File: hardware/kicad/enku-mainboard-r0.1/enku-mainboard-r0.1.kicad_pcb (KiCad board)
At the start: 4 copper layers, 54 x 94 mm, 156 parts, among them J1 1S LiPo + NTC, J2 Hirose DM3AT-SF-PEJM5, J3 FH34SRJ-24S-0.5SH(50), J4 FH34SRJ-6S-0.5SH(50), J5 GCT USB4105-GF-A-120, J6 4-pin pogo dock, J7 Tag-Connect TC2030-IDC-NL, J8 Pro Wireless Qi raw interface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, Q1 IRLML6346TRPBF, Q2 BSS138LT1G, Q3 BSS138LT1G, SW1 HARD POWER, SW2 BOOT / RECOVERY, SW3 BTN_PREV, SW4 BTN_NEXT, SW5 BTN_SELECT, SW6 BTN_BACK, U1 ESP32-S3-WROOM-1-N16R8, U2 TPS2121, U3 BQ25185DLHR, U4 TPS63802DLAR, U5 BMI270, U6 DRV5032FBDBZR, U7 TPS923610DRLR, U8 USBLC6-2SC6

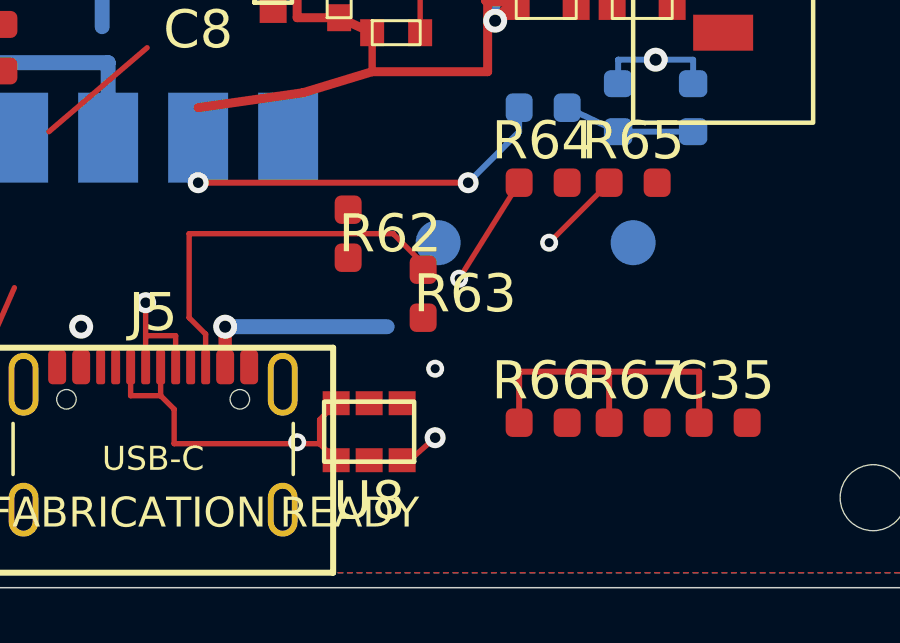
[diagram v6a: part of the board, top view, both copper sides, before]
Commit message: pcb: purge orphaned USB differential stubs
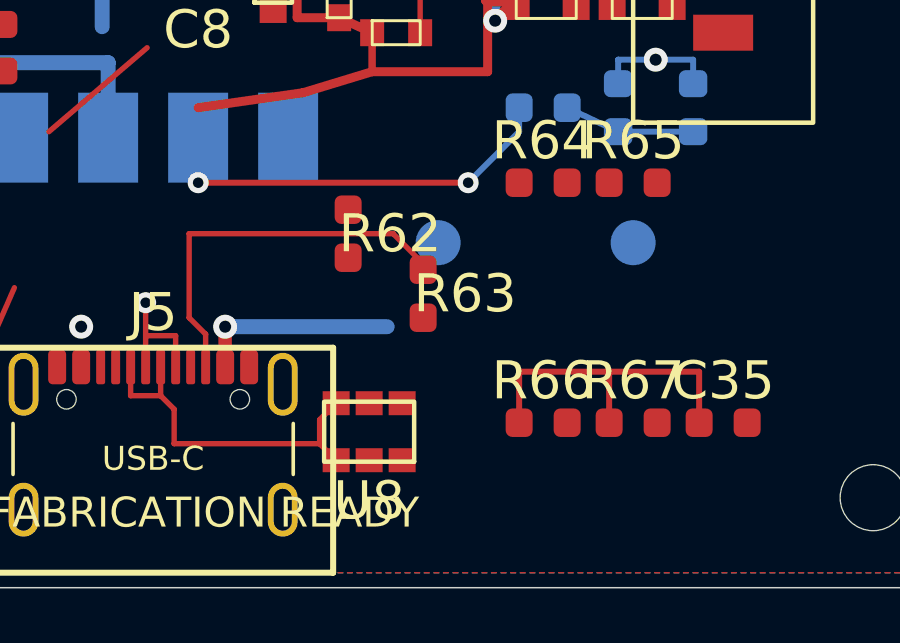
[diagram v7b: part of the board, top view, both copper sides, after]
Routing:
- net USB_DP_CONN: track 9.35 -> 4.19 mm, vias 4 -> 1
- net USB_DM_CONN: track 14.7 -> 11.9 mm, vias 2 -> 0
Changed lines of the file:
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@@
   (segment (start 46.75 105.60) (end 46.75 104.50) (width 0.18) (layer "F.Cu") (net 6))
   (via (at 46.75 104.50) (size 0.70) (drill 0.35) (layers "F.Cu" "B.Cu") (net 6))
-  (via (at 56.40 109.00) (size 0.70) (drill 0.35) (layers "F.Cu" "B.Cu") (net 6))
-  (segment (start 56.40 109.00) (end 55.55 109.75) (width 0.18) (layer "F.Cu") (net 6))
-  (segment (start 55.55 109.75) (end 55.30 109.75) (width 0.18) (layer "F.Cu") (net 6))
   (segment (start 46.25 106.645) (end 46.25 107.60) (width 0.18) (layer "F.Cu") (net 7))
   (segment (start 47.25 106.645) (end 47.25 107.60) (width 0.18) (layer "F.Cu") (net 7))
@@
   (segment (start 62.2 106.8) (end 65.2 106.8) (width 0.20) (layer "F.Cu") (net 8))
   (segment (start 65.2 106.8) (end 65.2 108.5) (width 0.20) (layer "F.Cu") (net 8))
-  (via (at 56.4 106.7) (size 0.60) (drill 0.30) (layers "F.Cu" "In1.Cu") (net 6))
   (segment (start 53.1 107.85) (end 52.55 108.4) (width 0.18) (layer "F.Cu") (net 7))
   (segment (start 52.55 108.4) (end 52.55 109.2) (width 0.18) (layer "F.Cu") (net 7))
-  (via (at 57.2 103.7) (size 0.60) (drill 0.30) (layers "F.Cu" "In1.Cu") (net 6))
-  (segment (start 57.2 103.7) (end 59.2 100.5) (width 0.18) (layer "F.Cu") (net 6))
-  (via (at 51.8 109.15) (size 0.60) (drill 0.30) (layers "F.Cu" "In1.Cu") (net 7))
-  (via (at 60.2 102.5) (size 0.60) (drill 0.30) (layers "F.Cu" "In1.Cu") (net 7))
-  (segment (start 60.2 102.5) (end 62.2 100.5) (width 0.18) (layer "F.Cu") (net 7))
   (segment (start 30.825 104) (end 25 100.6) (width 0.18) (layer "F.Cu") (net 10))
   (via (at 70.5 33.5) (size 0.60) (drill 0.30) (layers "F.Cu" "B.Cu") (net 13))

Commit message: pcb: purge isolated EPD service vias
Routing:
- net EPD_VSL: track 1.55 -> 0.00 mm, vias 2 -> 0
- net EPD_VSH2: track 1.55 -> 0.00 mm, vias 2 -> 0
- net EPD_RESE: vias 3 -> 1
- net EPD_GDR: vias 1 -> 0
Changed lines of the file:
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@@
   (segment (start 52.55 108.4) (end 52.55 109.2) (width 0.18) (layer "F.Cu") (net 7))
   (segment (start 30.825 104) (end 25 100.6) (width 0.18) (layer "F.Cu") (net 10))
-  (via (at 70.5 33.5) (size 0.60) (drill 0.30) (layers "F.Cu" "B.Cu") (net 13))
   (via (at 62.75 25.5) (size 0.60) (drill 0.30) (layers "F.Cu" "In1.Cu") (net 14))
   (segment (start 62.75 25.5) (end 69.5 25.5) (width 0.18) (layer "In1.Cu") (net 14))
-  (via (at 71 29.05) (size 0.60) (drill 0.30) (layers "F.Cu" "In1.Cu") (net 14))
-  (via (at 72 31.8) (size 0.60) (drill 0.30) (layers "F.Cu" "B.Cu") (net 14))
   (segment (start 51.8 28.4) (end 48.4 27.775) (width 0.18) (layer "F.Cu") (net 24))
-  (via (at 52.2 30.2) (size 0.60) (drill 0.30) (layers "F.Cu" "In2.Cu") (net 27))
-  (via (at 60.2 34.5) (size 0.60) (drill 0.30) (layers "F.Cu" "In2.Cu") (net 27))
-  (segment (start 60.2 34.5) (end 60.2 32.95) (width 0.18) (layer "F.Cu") (net 27))
-  (via (at 61.75 28) (size 0.60) (drill 0.30) (layers "F.Cu" "In2.Cu") (net 15))
-  (via (at 58 34.5) (size 0.60) (drill 0.30) (layers "F.Cu" "In2.Cu") (net 15))
-  (segment (start 58 34.5) (end 58 32.95) (width 0.18) (layer "F.Cu") (net 15))
   (segment (start 63.8001 44.5) (end 62.95 42.0) (width 0.25) (layer "F.Cu") (net 36))
 )
